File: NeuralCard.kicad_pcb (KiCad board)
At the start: 2 copper layers, 85.6 x 54 mm, 53 parts, among them J1 ProgPads, SW1 SW-SMD_4P-L5.1-W5.1-P3.70-LS6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, SW2 SW-SMD_4P-L5.1-W5.1-P3.70-LS6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, U1 WIRELM-SMD_ESP32-S3-WROOM-1, U2 LGA-14_L3.0-W2.5-P0.50-TL, U4 SO-8_L4.9-W3.9-P1.27-LS5.9-BL

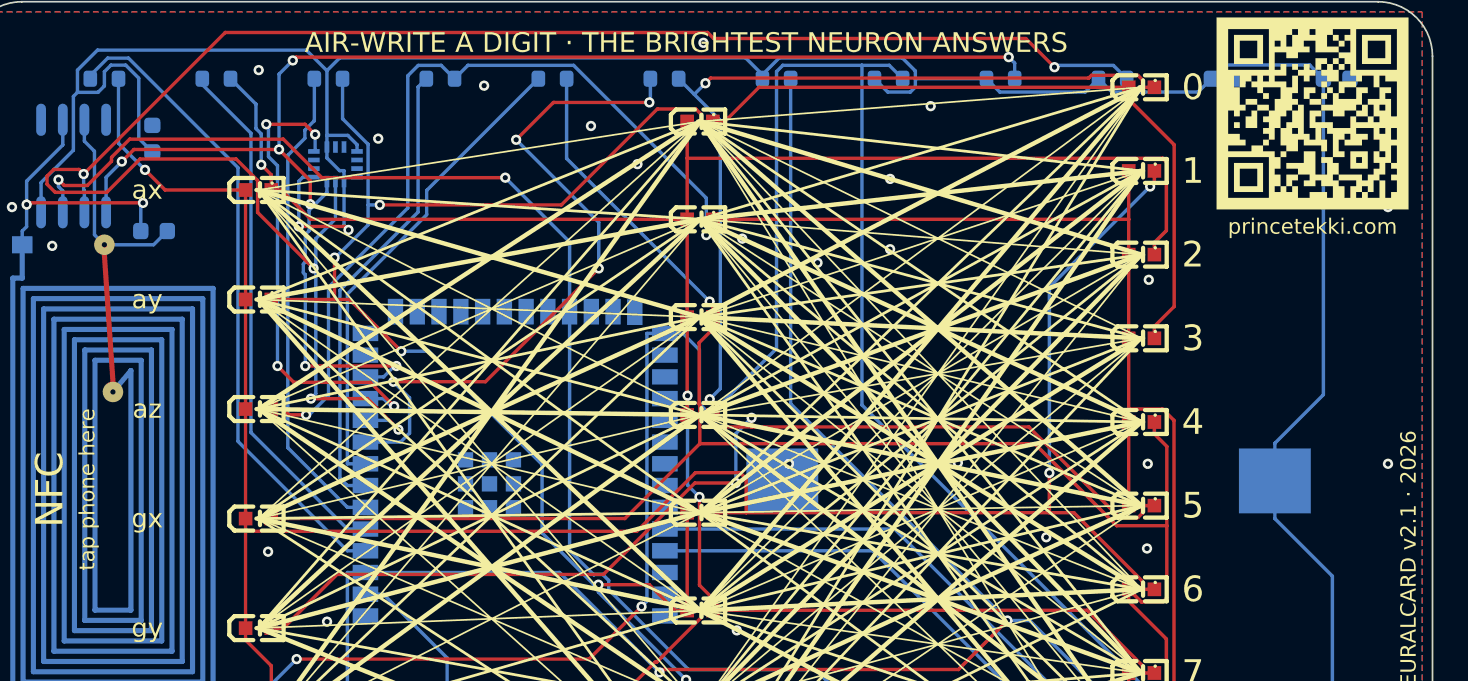
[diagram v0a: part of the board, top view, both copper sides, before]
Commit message: fix: repair grounds, add hardware power switch, clean DRC
- Fix stranded grounds: NFC chip (U4) and IMU (U2) had B.Cu SMD GND pads
  connected only through isolated pour fragments; add stitching vias + short
  tracks tying them into the main plane
- Remove 16 isolated-copper islands and 7 degenerate zero-area zones; set GND
  zones to remove-islands; add F/B GND plane stitching vias
- Add hardware slide power switch (SW3) in series with the coin cell +
  terminal: BT1(+) -> VBAT -> SW3 common -> SW3 on -> +3V3 rail, so the card
  is no longer always-on (true off, zero drain)
- Attach a 3D model to SW3 (scaled slide-switch stand-in)
- Configure silk-over-copper / silk-overlap / text DRC as intentional (neural-
  net artwork) and clip silk to solder mask at gerber output
- Set min through-hole/via/clearance rules to match fine stitching
- Regenerate gerbers + JLCPCB zip; add SW3 to BOM

Result: 0 DRC violations (only 1 cosmetic GND pour-fragment ratsnest remains).
Note: SW3 uses a generic 3-pad footprint + stand-in 3D model; match to a
specific tiny SMD slide switch and verify pad pitch before production.
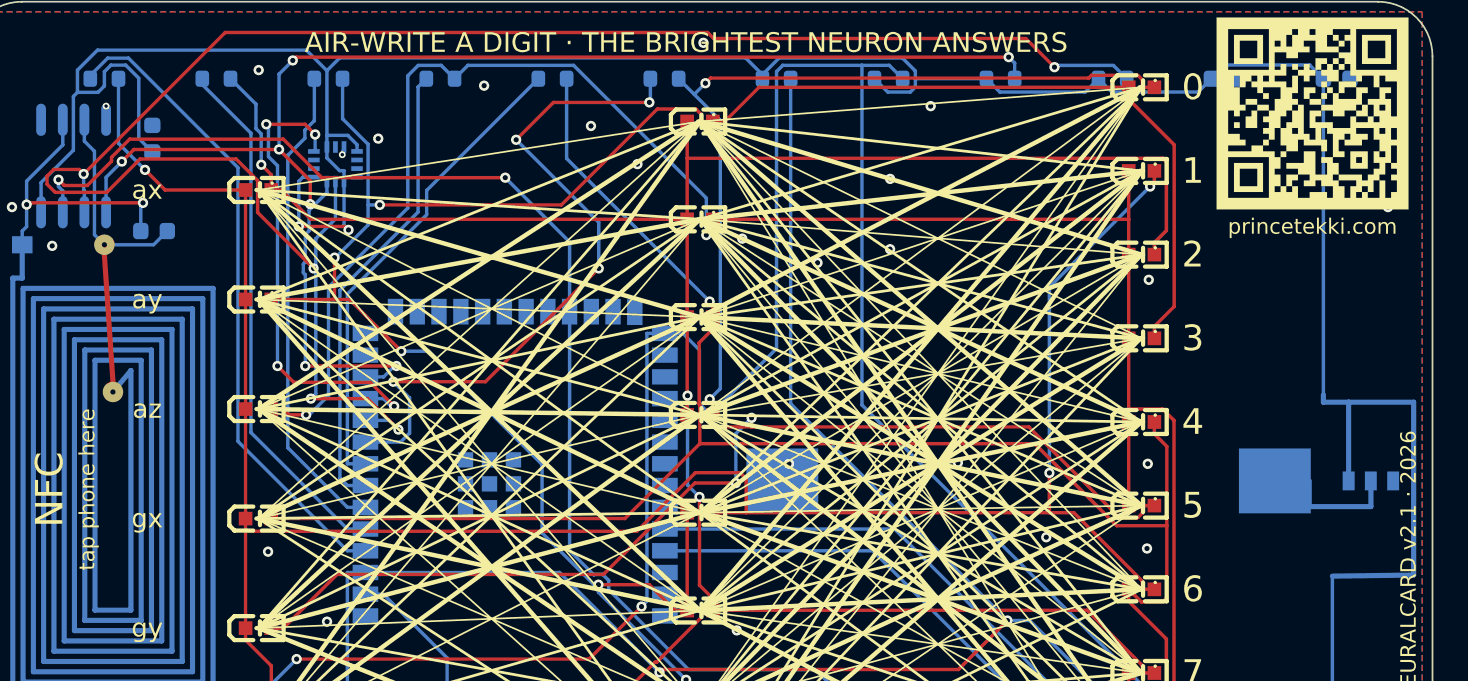
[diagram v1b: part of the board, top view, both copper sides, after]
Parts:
- added SW3: , , B.Cu at (82.0, 28.0)
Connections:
- BT1 pad 1: +3V3 -> VBAT
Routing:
- net +3V3: track 266.3 -> 278.3 mm
- net VBAT: track 0.00 -> 6.60 mm
- net GND: track 0.00 -> 1.26 mm, vias 33 -> 34

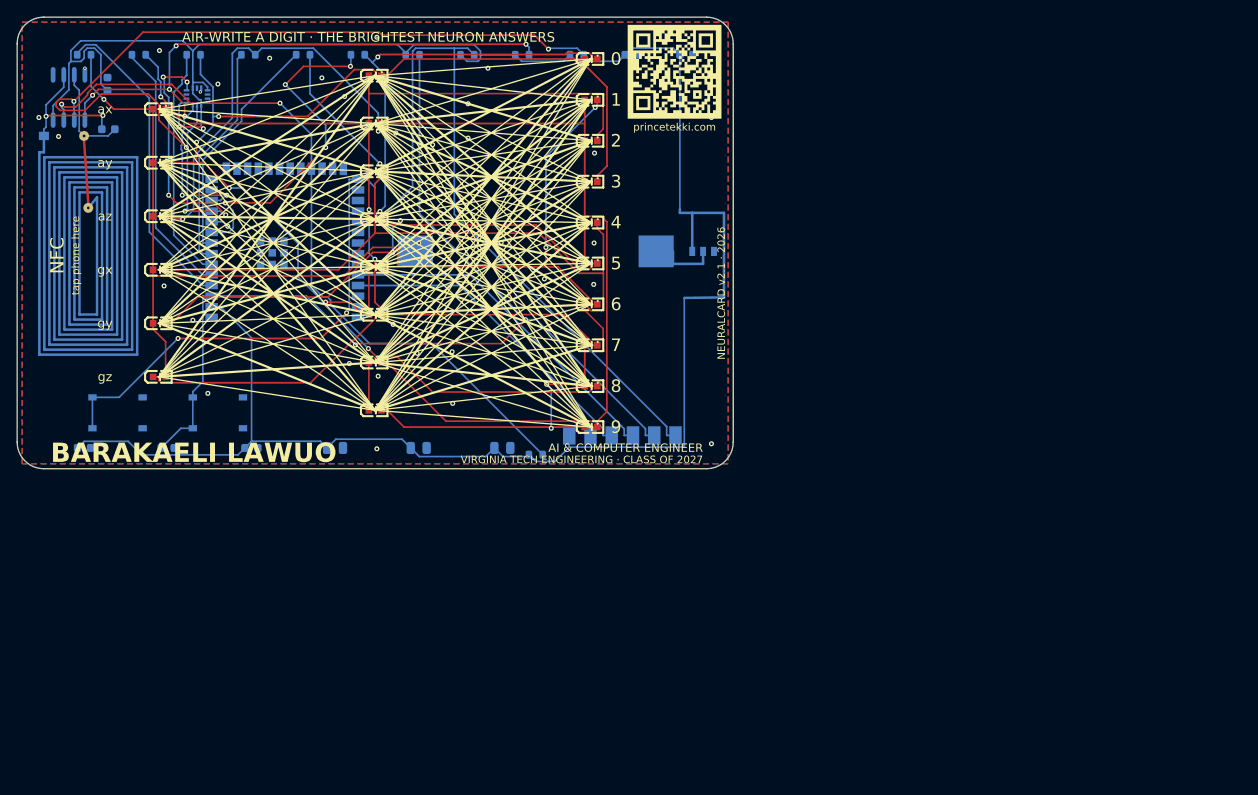
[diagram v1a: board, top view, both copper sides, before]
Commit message: fix: replace improvised SW3 land with official MSK12C02 footprint
JLCPCB rejected SW3 at DFM on order SMT026072863054: the part they had
selected, C431540 (SHOU HAN MSK12C02), does not fit the pads on the board.

SW3 was added by hand in b2ccb56 and never went through the generator, so it
carried an improvised land pattern -- three 0.7x1.1mm pads on 1.3mm pitch, no
mounting tabs, no locating holes, and a placeholder 3D model (a Copal DIP
switch scaled to 0.62). The real MSK12C02 is 8x2.8mm and needs four shield
tabs plus two 0.85mm NPTH locating holes. Nothing was going to seat on that
land. The BOM had the part as "select-at-order" with a note to verify the
footprint against whatever got chosen; that verification never happened.

Swaps in Button_Switch_SMD:SW_SPDT_Shouhan_MSK12C02, the KiCad library
footprint drawn from the manufacturer datasheet. The part is right-angle, so
it is rotated 270 deg with its pins facing inboard toward BT1 and the actuator
facing the right card edge where a thumb can reach it, and moved 0.546mm
inboard to leave 1.0mm from courtyard to board edge for assembly.

Net mapping is unchanged from the schematic: pad 2 is the common pole on VBAT,
pad 3 the closed throw on +3V3, pad 1 the open throw. The four SH tabs are
left netless -- they are the retention frame, and the datasheet does not state
that it is isolated from the contacts, so tying them to GND risks shorting the
coin cell. They still solder down for mechanical retention.

DRC is clean under the project rules (0 violations, 0 unconnected). Measured
against the same ruleset, the board carries exactly the same silk-art
violation count as before this change.

Fab package regenerated: both NPTH holes now appear in the drill file at
X142.111 Y-62.943 and Y-65.943, and the CPL places SW3 at 142.1112,-64.4434
rotated -90. BOM now names C431540 outright instead of select-at-order.

Adds tools/fix_sw3_footprint.py documenting the swap and tools/export_fab.py
so a fab refresh is one reproduci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
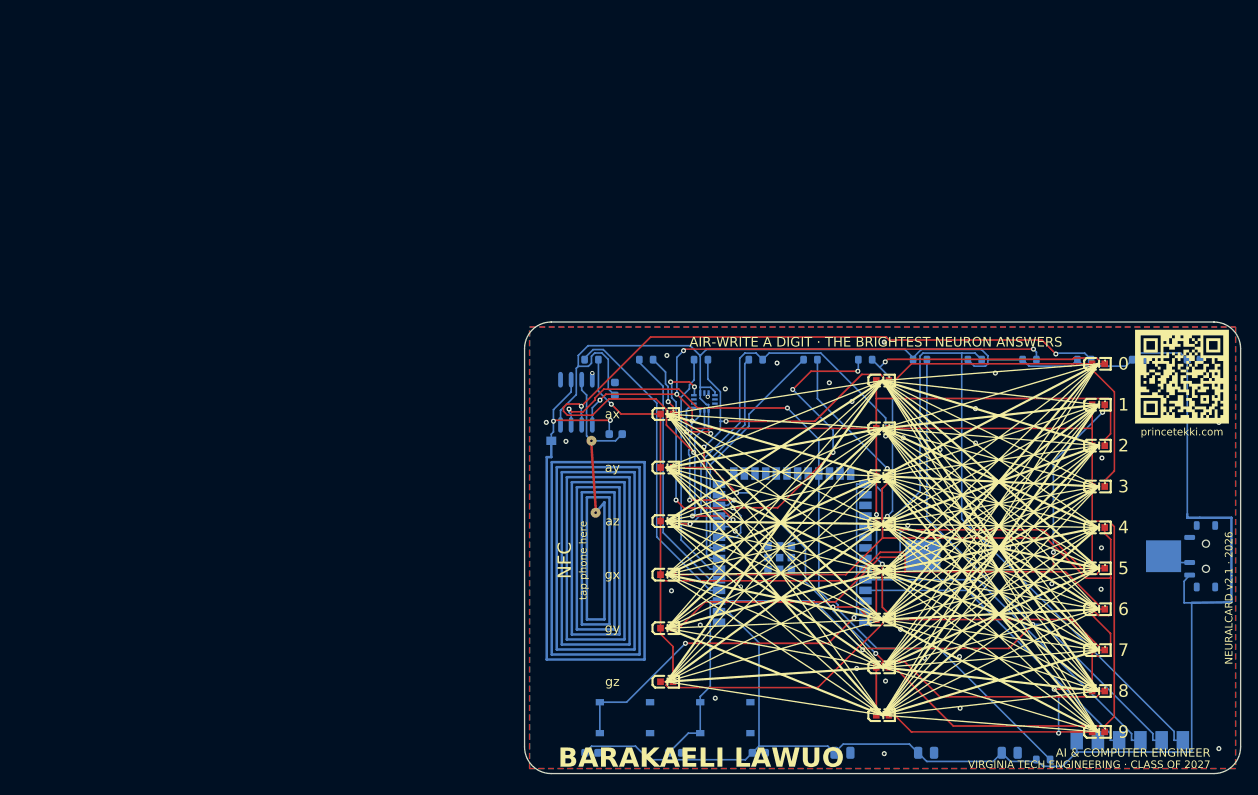
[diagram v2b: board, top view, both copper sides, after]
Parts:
- SW3: value (none) -> MSK12C02; footprint (none) -> SW_SPDT_Shouhan_MSK12C02
- moved C2 70.8 mm to (140.7, 40.9)
- moved D15 70.8 mm to (129.3, 41.4)
- moved D16 70.8 mm to (129.3, 46.3)
- moved D17 70.8 mm to (129.3, 51.2)
- moved D18 70.8 mm to (129.3, 56.1)
- moved D19 70.8 mm to (129.3, 61.0)
- moved D20 70.8 mm to (129.3, 65.9)
- moved D21 70.8 mm to (129.3, 70.8)
- moved D22 70.8 mm to (129.3, 75.7)
- moved D23 70.8 mm to (129.3, 80.6)
- moved D24 70.8 mm to (129.3, 85.4)
- moved ANT1 70.8 mm to (60.7, 36.4)
- moved BT1 70.8 mm to (122.7, 64.4)
- moved C1 70.8 mm to (134.1, 40.9)
- moved C10 70.8 mm to (118.7, 87.9)
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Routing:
- net VBAT: track 6.60 -> 2.16 mm
- net GND: vias 34 -> 35

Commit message: feat: v2.2 decoupling replace
Board revision driven by the kicad-happy analysis. The headline is decoupling.

place_pcb.py dealt every passive into two cosmetic edge rows by list order,
ignoring which IC each cap served. The caps were correctly wired and completely
ineffective: the ESP32's nearest cap was 24.8mm away and the IMU's own C5 was
42mm away. At 0.3-0.8nH of loop inductance per mm that does nothing at the
frequencies that matter, and neither ERC nor DRC can see it because the
connectivity was always correct.

C1/C2 now flank the module, C3/C4/C8 sit in the 6mm corridor beside it rotated
90deg to fit, C5 is 4mm from the IMU. U1 goes 24.8 -> 11.4mm, U2 10.8 -> 4.0mm.
C9/C10 are 22uF ride-out rather than HF decoupling and stay in the edge row;
keeping them out of the corridor is what let the output-column charlieplex
lines route.

Also fixes SW3 missing from the placement table -- added by hand in b2ccb56, it
would have been dropped to the default centre slot by this re-place, silently
undoing the DFM fix. And six scripts hardcoded ~/kicad-projects/NeuralCard,
which is not where the project lives; stitch_islands.py failed outright on the
first run because of it.

Verification: 100% routed (freerouting score 995.36, zero unrouted), 0
unconnected pads (the 7 reported are netless by design -- ANT1's escape and
SW3's 2 NPTH plus 4 shield tabs), 631 tracks and 79 vias, ERC 0 errors, DRC 0
clearance and 0 crossing violations, CPL still 52 placements.

Known regression: isolated GND pour islands 5 -> 28. Redundant copper the
stitcher cannot reach with a via; every GND pad is track-routed so it is
cosmetic, and stitch_islands.py converges there. Worth revisiting before a
production run.

Supersedes the v2.1 fab package. Order SMT026072863054 was placed against v2.1.
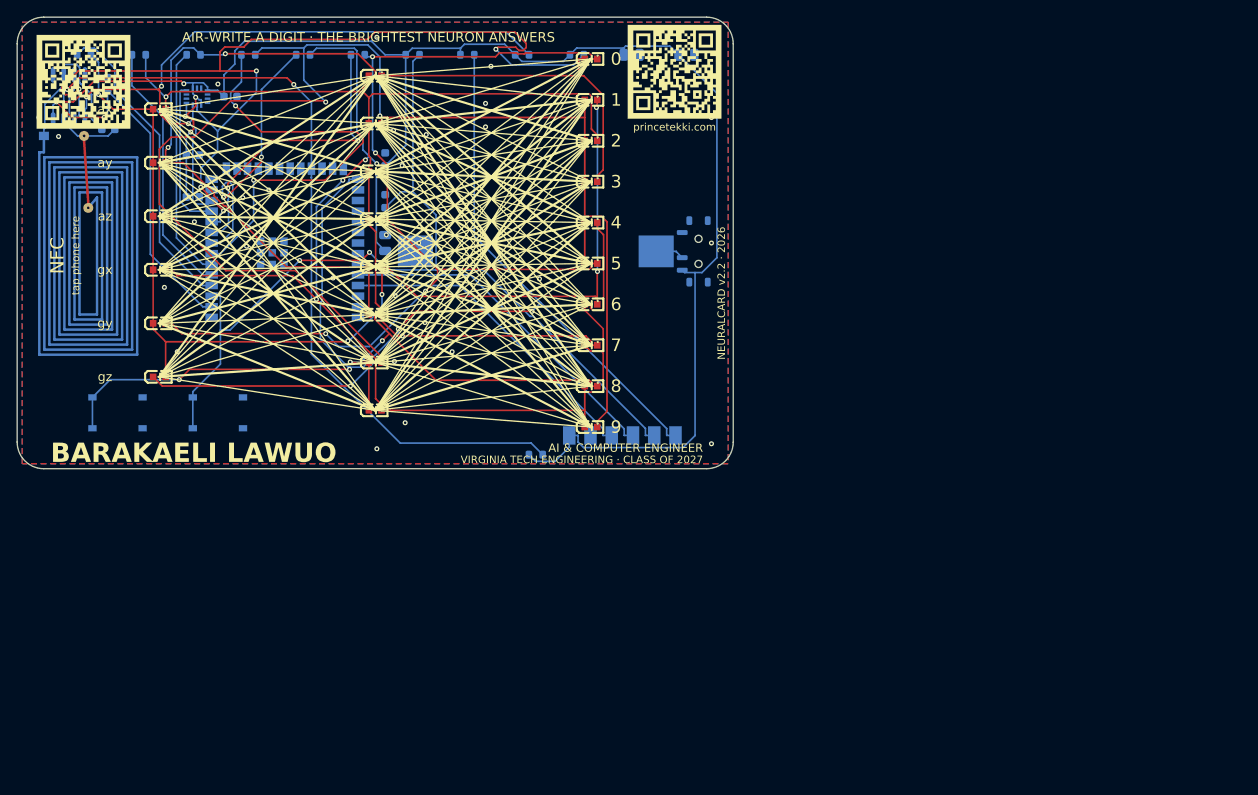
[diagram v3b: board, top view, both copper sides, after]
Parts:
- SW3: value MSK12C02 -> SW_SPDT_Shouhan_MSK12C02
- moved C2 121.2 mm to (21.0, 21.5)
- moved C1 115.7 mm to (21.0, 16.5)
- moved C5 100.7 mm to (25.5, 9.50)
- moved C10 92.0 mm to (80.0, 4.50)
- moved C9 90.6 mm to (73.5, 4.50)
- moved C8 81.9 mm to (44.0, 27.0), turned to 90 degrees
- moved C3 75.1 mm to (44.0, 17.0), turned to 90 degrees
- moved C4 74.5 mm to (44.0, 22.0), turned to 90 degrees
- moved D15 70.8 mm to (68.6, 5.00)
- moved D16 70.8 mm to (68.6, 9.89)
- moved D17 70.8 mm to (68.6, 14.8)
- moved D18 70.8 mm to (68.6, 19.7)
- moved D19 70.8 mm to (68.6, 24.6)
- moved D20 70.8 mm to (68.6, 29.4)
- moved D21 70.8 mm to (68.6, 34.3)
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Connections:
- SW3 pad 1: (no net) -> unconnected-(SW3-A-Pad1)
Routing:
- net +3V3: track 278.1 -> 248.7 mm, vias 2 -> 6
- net CHX4: track 27.1 -> 50.6 mm, vias 0 -> 2
- net CP4: track 149.9 -> 167.5 mm
- net IMU_INT: track 28.2 -> 18.2 mm, vias 4 -> 0
- net NFC_GPO: track 90.1 -> 97.6 mm
- net CP5: track 143.5 -> 136.4 mm, vias 3 -> 4
- net EN: track 121.8 -> 114.8 mm
- net CHX6: track 40.5 -> 35.7 mm, vias 4 -> 2
- net CHX5: track 28.2 -> 32.3 mm, vias 0 -> 2
- net IO0: track 149.0 -> 144.9 mm, vias 2 -> 4
- net NFC_ANT_A: track 16.8 -> 20.1 mm, vias 2 -> 0
- net SCL: track 112.4 -> 114.9 mm
- net CP6: track 113.5 -> 115.9 mm
- net CP3: track 163.6 -> 161.7 mm, vias 5 -> 4
- net CP1: track 128.2 -> 129.6 mm, vias 3 -> 5
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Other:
- board text added: "NEURALCARD v2.2 · 2026"
- board text added: "NeuralCard v2.2 · princetekki.com"
- board text removed: "NEURALCARD v2.1 · 2026"
- board text removed: "NeuralCard v2.1 · princetekki.com"
